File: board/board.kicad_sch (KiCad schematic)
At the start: 1 part

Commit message: initial
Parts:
- added J1: 019_100BASE-T_2x5, on_edge:on_edge_2x05_device, symbol put_on_edge:019_100BASE-T_with_CT
- added J2: 011_GPIO, on_edge:on_edge_2x05_device, symbol put_on_edge:011_GPIO
- added J3: PoE, on_edge:on_edge_2x05_host, symbol put_on_edge:013_PoE_rectified
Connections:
- new net GND: J1.1 (GND), J1.6 (GND), J2.1 (GND), J2.8 (GND)
- new net PoE_GND: J3.1 (GND), J3.2 (GND), J3.5 (GND)
- new net eth_conn/LED1+: J2.2 (GPIO0)
- new net eth_conn/LED1-: J2.3 (GPIO1)
- new net eth_conn/LED2+: J2.4 (GPIO2)
- new net eth_conn/LED2-: J2.5 (GPIO3)
- new net eth_conn/RCT: J1.8 (CT2)
- new net eth_conn/RD+: J1.4 (TD2+)
- new net eth_conn/RD-: J1.5 (TD2-)
- new net eth_conn/TCT: J1.7 (CT1)
- new net eth_conn/TD+: J1.2 (TD1+)
- new net eth_conn/TD-: J1.3 (TD1-)
- new net eth_conn/VC1+: J3.3 (48V), J3.4 (48V)
- no-connect marks 0 -> 4
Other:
- sheet implementation renamed eth_conn
- sheet eth_conn: file implementation.kicad_sch -> eth_conn.kicad_sch
- sheet eth_conn ports: added LED1+, LED1-, LED2+, LED2-, RCT, RD+, RD-, TCT, TD+, TD-, VC1+, VC1-; removed none
- note removed: "Input connectors go here"
- note removed: "Output connectors go here"

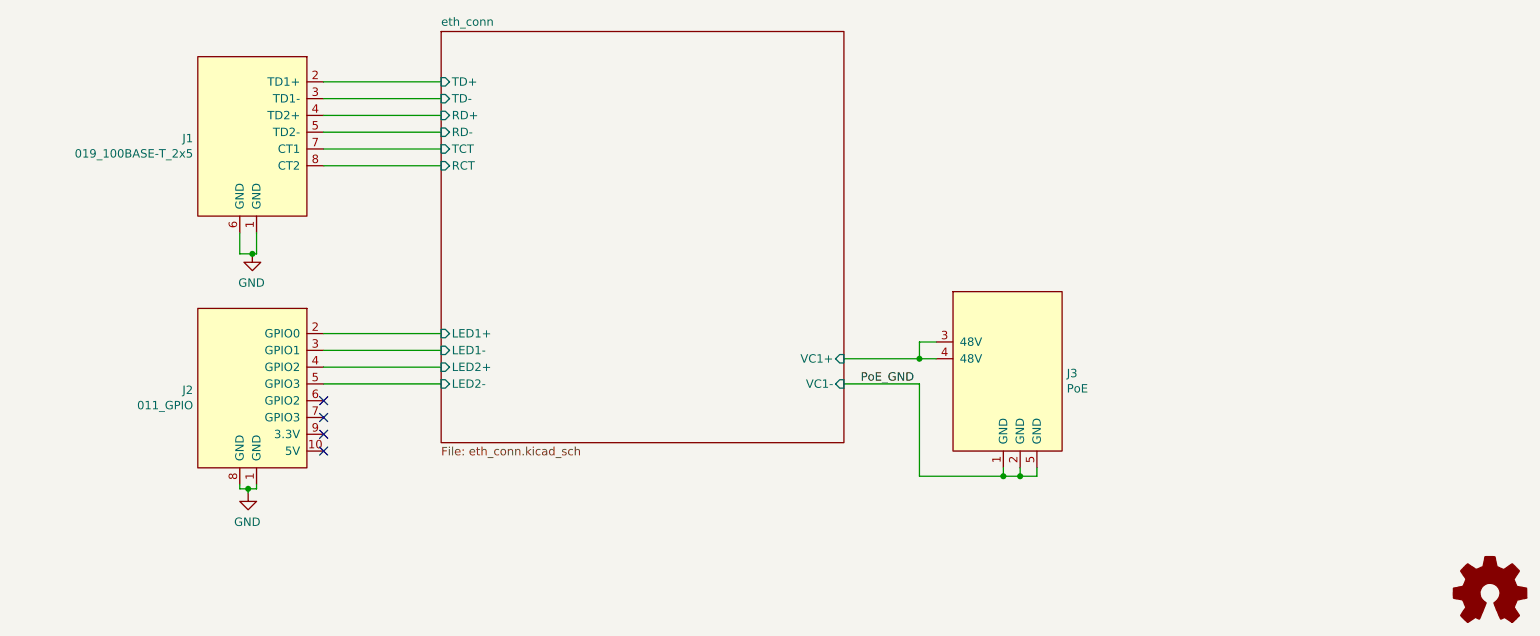
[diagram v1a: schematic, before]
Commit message: modernized to new put_on_edge connectors with 3.3 and 5v
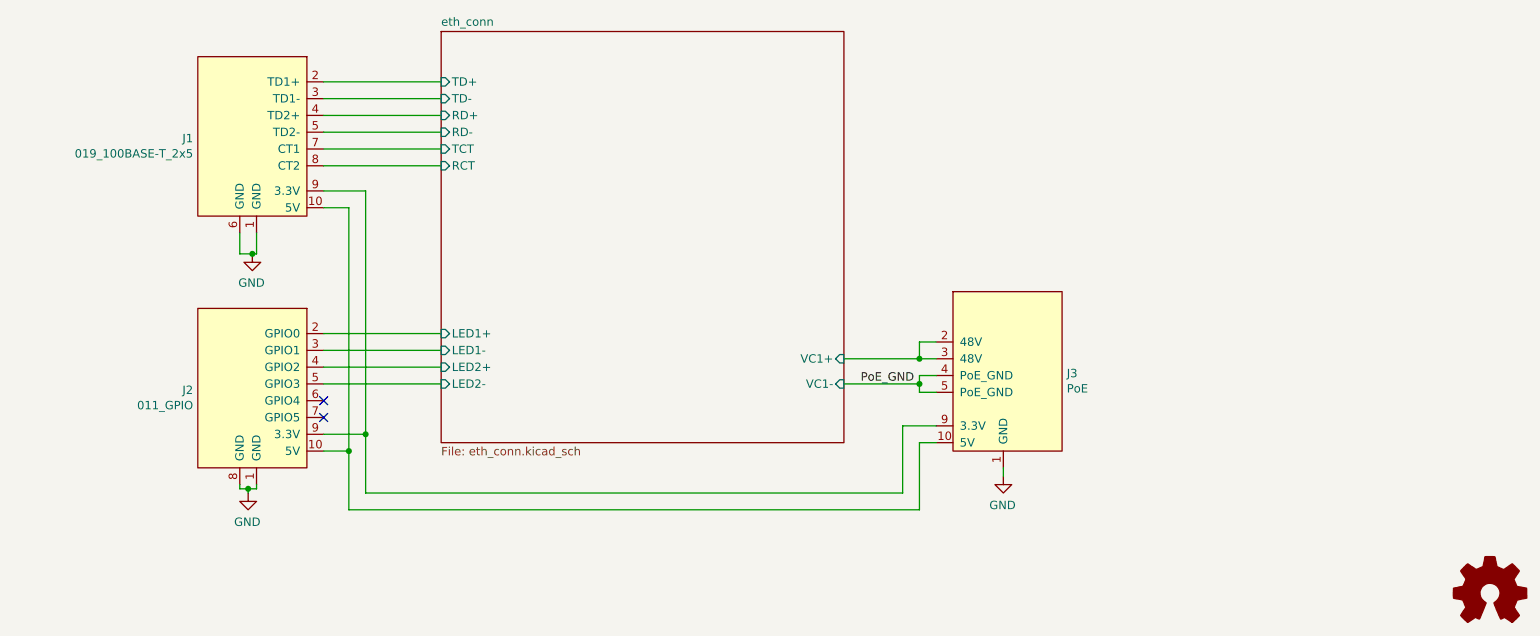
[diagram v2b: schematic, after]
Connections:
- net GND: now also J3.1 (GND)
- net PoE_GND: now also J3.4 (PoE_GND); no longer J3.1 (GND), J3.2 (GND)
- net eth_conn/VC1+: now also J3.2 (48V); no longer J3.4 (48V)
- net at J2.10 (5V): now also J1.10 (5V), J3.10 (5V)
- net at J2.9 (3.3V): now also J1.9 (3.3V), J3.9 (3.3V)
- no-connect marks 4 -> 2
